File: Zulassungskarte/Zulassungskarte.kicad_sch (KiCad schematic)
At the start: 31 parts, among them J1 Conn_02x04_Counter_Clockwise, J2 Conn_02x04_Counter_Clockwise, U1 ATmega48V-10AU

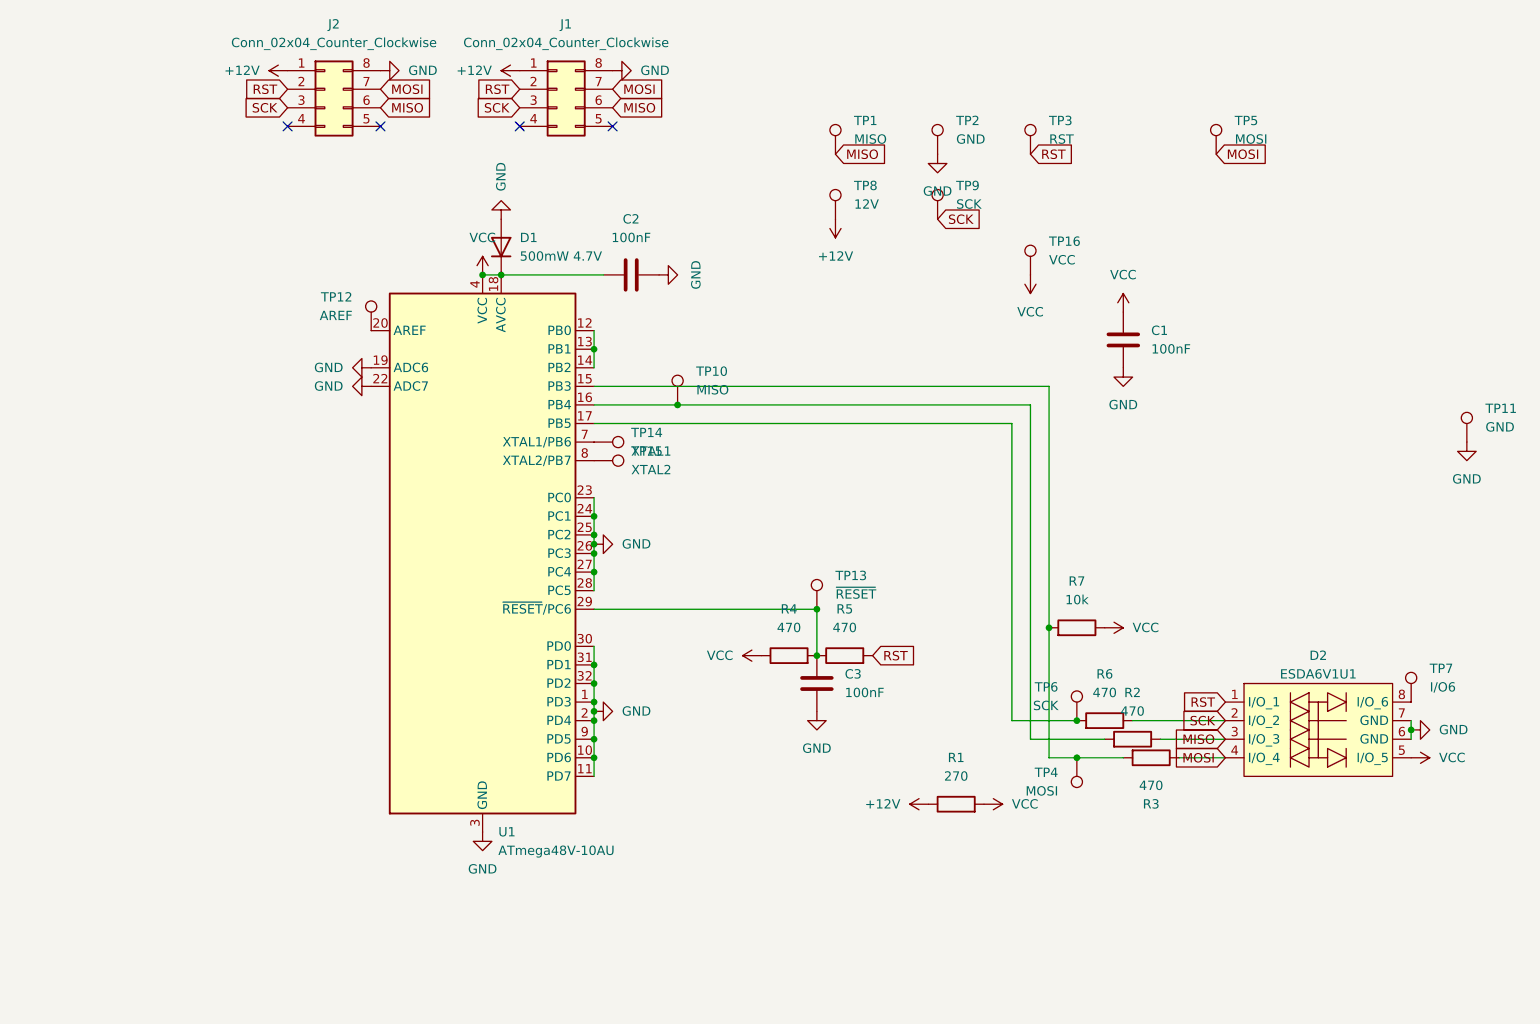
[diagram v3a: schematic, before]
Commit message: arduino isp und anschluss der normal am halter ist
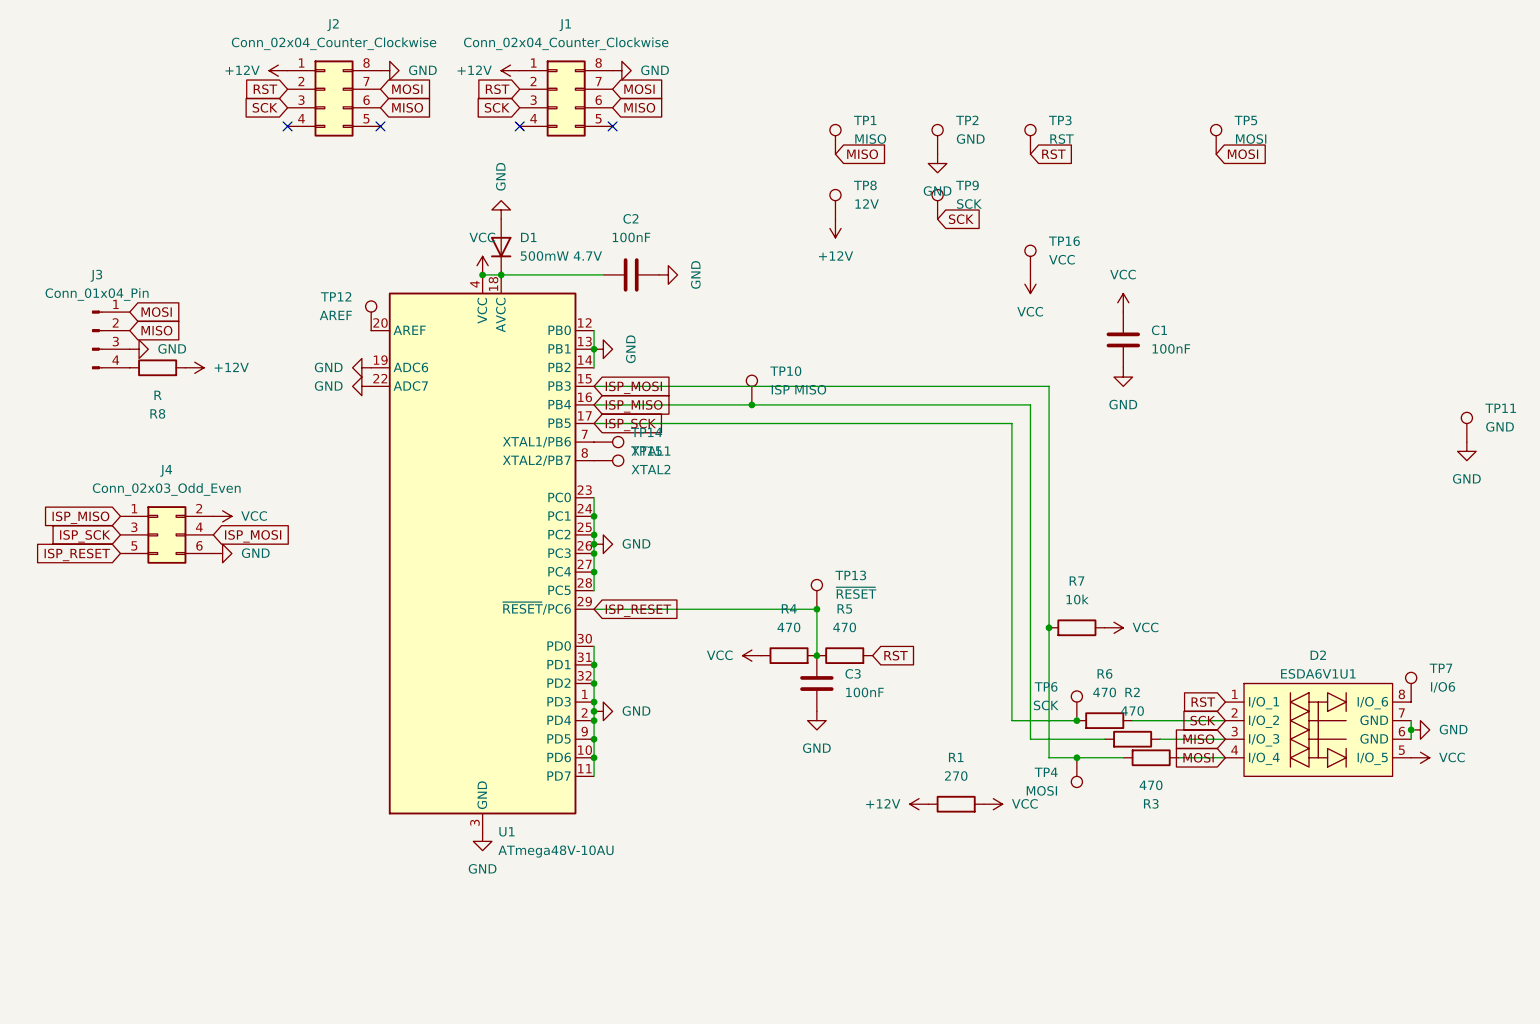
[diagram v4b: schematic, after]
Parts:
- added J3: Conn_01x04_Pin, Connector_JST:JST_XH_S4B-XH-A-1_1x04_P2.50mm_Horizontal, symbol Connector:Conn_01x04_Pin
- added J4: Conn_02x03_Odd_Even, Connector_IDC:IDC-Header_2x03_P2.54mm_Vertical, symbol Connector_Generic:Conn_02x03_Odd_Even
- added R8: R, Resistor_SMD:R_0805_2012Metric, symbol Device:R
- TP10: value MISO -> ISP MISO
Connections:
- net +12V: now also R8.2
- net GND: now also U1.12 (PB0), U1.13 (PB1), U1.14 (PB2), J3.3 (Pin_3), J4.6 (Pin_6)
- net MISO: now also J3.2 (Pin_2)
- net MOSI: now also J3.1 (Pin_1)
- net VCC: now also J4.2 (Pin_2)
- net ISP_MOSI: now reaches R3.2, R7.2, TP4.1, U1.15 (PB3)
- net ISP_MOSI: now also J4.4 (Pin_4)
- net ISP_MISO: now reaches R2.2, TP10.1, U1.16 (PB4)
- net ISP_MISO: now also J4.1 (Pin_1)
- net ISP_SCK: now reaches R6.2, TP6.1, U1.17 (PB5)
- net ISP_SCK: now also J4.3 (Pin_3)
- net ISP_RESET: now reaches C3.1, R4.2, R5.1, TP13.1, U1.29 (~{RESET}/PC6)
- net ISP_RESET: now also J4.5 (Pin_5)
- new net: J3.4 (Pin_4), R8.1
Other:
- moved on the sheet: TP10

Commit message: 5v und loecher
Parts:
- added FID1, FID2, FID3: Fiducial, Fiducial:Fiducial_0.75mm_Mask2.25mm, symbol Mechanical:Fiducial
- added H1, H2, H3: MountingHole, MountingHole:MountingHole_3.2mm_M3, symbol Mechanical:MountingHole
- J3: footprint Connector_JST:JST_XH_S4B-XH-A-1_1x04_P2.50mm_Horizontal -> Connector_PinHeader_2.54mm:PinHeader_1x04_P2.54mm_Vertical
- R8: footprint Resistor_SMD:R_0805_2012Metric -> Resistor_SMD:R_0603_1608Metric_Pad0.98x0.95mm_HandSolder
- TP14, TP15: footprint TestPoint:TestPoint_Pad_D1.5mm -> TestPoint:TestPoint_Pad_D1.0mm
- U1: value ATmega48V-10AU -> ATmega48
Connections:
- net +12V renamed +5V

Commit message: zlk
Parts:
- J3, J4: now not fitted
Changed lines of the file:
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@@
 		(in_bom yes)
 		(on_board yes)
-		(dnp no)
+		(dnp yes)
 		(fields_autoplaced yes)
 		(property "Reference" "J3"
@@
 		(in_bom yes)
 		(on_board yes)
-		(dnp no)
+		(dnp yes)
 		(fields_autoplaced yes)
 		(property "Reference" "J4"

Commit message: 12v zlk
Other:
- moved on the sheet: C2, D1
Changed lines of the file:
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@@
 	)
 	(junction
-		(at 72.39 49.53)
-		(diameter 0)
-		(color 0 0 0 0)
-	)
-	(junction
 		(at 87.63 59.69)
 		(diameter 0)
@@
 	)
 	(junction
-		(at 74.93 49.53)
+		(at 87.63 105.41)
 		(diameter 0)
 		(color 0 0 0 0)
 	)
 	(junction
-		(at 87.63 105.41)
+		(at 87.63 109.22)
 		(diameter 0)
 		(color 0 0 0 0)
 	)
 	(junction
-		(at 87.63 109.22)
+		(at 73.66 49.53)
 		(diameter 0)
 		(color 0 0 0 0)
@@
 	(wire
 		(pts
-			(xy 72.39 49.53) (xy 74.93 49.53)
-		)
-		(stroke
-			(width 0)
-			(type default)
-		)
-	)
-	(wire
-		(pts
 			(xy 157.48 113.03) (xy 147.32 113.03)
 		)
@@
 	(wire
 		(pts
-			(xy 87.63 100.33) (xy 87.63 102.87)
+			(xy 73.66 49.53) (xy 74.93 49.53)
 		)
 		(stroke
@@
 	(wire
 		(pts
-			(xy 87.63 90.17) (xy 87.63 92.71)
+			(xy 87.63 100.33) (xy 87.63 102.87)
 		)
 		(stroke
@@
 	(wire
 		(pts
-			(xy 74.93 49.53) (xy 88.9 49.53)
+			(xy 87.63 90.17) (xy 87.63 92.71)
 		)
 		(stroke
@@
 	(wire
 		(pts
+			(xy 73.66 49.53) (xy 72.39 49.53)
+		)
+		(stroke
+			(width 0)
+			(type default)
+		)
+	)
+	(wire
+		(pts
 			(xy 87.63 107.95) (xy 87.63 105.41)
 		)
@@
 	(symbol
 		(lib_id "power:GND")
-		(at 74.93 41.91 0)
+		(at 102.87 135.89 270)
 		(mirror x)
 		(unit 1)
@@
 		(fields_autoplaced yes)
 		(property "Reference" "#PWR024"
-			(at 74.93 35.56 0)
+			(at 96.52 135.89 0)
 			(effects
 				(font
@@
 		)
 		(property "Value" "GND"
-			(at 74.9301 38.1 90)
+			(at 99.06 135.8899 90)
 			(effects
 				(font
@@
 		)
 		(property "Footprint" ""
-			(at 74.93 41.91 0)
+			(at 102.87 135.89 0)
 			(effects
 				(font
@@
 		)
 		(property "Datasheet" ""
-			(at 74.93 41.91 0)
+			(at 102.87 135.89 0)
 			(effects
 				(font
@@
 		)
 		(property "Description" "Power symbol creates a global label with name \"GND\" , ground"
-			(at 74.93 41.91 0)
+			(at 102.87 135.89 0)
 			(effects
 				(font
@@
 	(symbol
 		(lib_id "power:VCC")
-		(at 72.39 49.53 0)
+		(at 73.66 49.53 0)
 		(unit 1)
 		(exclude_from_sim no)
@@
 		(fields_autoplaced yes)
 		(property "Reference" "#PWR03"
-			(at 72.39 53.34 0)
+			(at 73.66 53.34 0)
 			(effects
 				(font
@@
 		)
 		(property "Value" "VCC"
-			(at 72.39 44.45 0)
+			(at 73.66 44.45 0)
 			(effects
 				(font
@@
 		)
 		(property "Footprint" ""
-			(at 72.39 49.53 0)
+			(at 73.66 49.53 0)
 			(effects
 				(font
@@
 		)
 		(property "Datasheet" ""
-			(at 72.39 49.53 0)
+			(at 73.66 49.53 0)
 			(effects
 				(font
@@
 		)
 		(property "Description" "Power symbol creates a global label with name \"VCC\""
-			(at 72.39 49.53 0)
+			(at 73.66 49.53 0)
 			(effects
 				(font
@@
 	)
 	(symbol
+		(lib_id "power:VCC")
+		(at 110.49 135.89 270)
+		(unit 1)
+		(exclude_from_sim no)
+		(in_bom yes)
+		(on_board yes)
+		(dnp no)
+		(fields_autoplaced yes)
+		(property "Reference" "#PWR08"
+			(at 106.68 135.89 0)
+			(effects
+				(font
+					(size 1.27 1.27)
+				)
+				(hide yes)
+			)
+		)
+		(property "Value" "VCC"
+			(at 114.3 135.8899 90)
+			(effects
+				(font
+					(size 1.27 1.27)
+				)
+				(justify left)
+			)
+		)
+		(property "Footprint" ""
+			(at 110.49 135.89 0)
+			(effects
+				(font
+					(size 1.27 1.27)
+				)
+				(hide yes)
+			)
+		)
+		(property "Datasheet" ""
+			(at 110.49 135.89 0)
+			(effects
+				(font
+					(size 1.27 1.27)
+				)
+				(hide yes)
+			)
+		)
+		(property "Description" "Power symbol creates a global label with name \"VCC\""
+			(at 110.49 135.89 0)
+			(effects
+				(font
+					(size 1.27 1.27)
+				)
+				(hide yes)
+			)
+		)
+		(pin "1"
+		)
+		(instances
+			(project "Zulassungskarte"
+				(path "/f437cf05-d297-460e-8639-991b777c08ac"
+					(reference "#PWR08")
+					(unit 1)
+				)
+			)
+		)
+	)
+	(symbol
 		(lib_id "power:GND")
 		(at 199.39 111.76 90)
@@
 	(symbol
 		(lib_id "Device:D")
-		(at 74.93 45.72 270)
-		(mirror x)
+		(at 106.68 135.89 0)
+		(mirror y)
 		(unit 1)
 		(exclude_from_sim no)
@@
 		(fields_autoplaced yes)
 		(property "Reference" "D1"
-			(at 77.47 44.4499 90)
+			(at 105.4099 133.35 90)
 			(effects
 				(font
@@
 		)
 		(property "Value" "500mW 4.7V"
-			(at 77.47 46.9899 90)
+			(at 107.9499 133.35 90)
 			(effects
 				(font
@@
 		)
 		(property "Footprint" "Diode_SMD:D_SOD-123"
-			(at 74.93 45.72 0)
+			(at 106.68 135.89 0)
 			(effects
 				(font
@@
 		)
 		(property "Datasheet" "~"
-			(at 74.93 45.72 0)
+			(at 106.68 135.89 0)
 			(effects
 				(font
@@
 		)
 		(property "Description" "Diode"
-			(at 74.93 45.72 0)
+			(at 106.68 135.89 0)
 			(effects
 				(font
@@
 		)
 		(property "Sim.Device" "D"
-			(at 74.93 45.72 0)
+			(at 106.68 135.89 0)
 			(effects
 				(font
@@
 		)
 		(property "Sim.Pins" "1=K 2=A"
-			(at 74.93 45.72 0)
+			(at 106.68 135.89 0)
 			(effects
 				(font
@@
 	(symbol
 		(lib_id "Device:C")
-		(at 92.71 49.53 90)
+		(at 173.99 58.42 0)
 		(unit 1)
 		(exclude_from_sim no)
@@
 		(fields_autoplaced yes)
 		(property "Reference" "C2"
-			(at 92.71 41.91 90)
+			(at 181.61 58.42 90)
 			(effects
 				(font
@@
 		)
 		(property "Value" "100nF"
-			(at 92.71 44.45 90)
+			(at 179.07 58.42 90)
 			(effects
 				(font
@@
 		)
 		(property "Footprint" "Capacitor_SMD:C_0805_2012Metric_Pad1.18x1.45mm_HandSolder"
-			(at 96.52 48.5648 0)
+			(at 174.9552 62.23 0)
 			(effects
 				(font
@@
 		)
 		(property "Datasheet" "~"
-			(at 92.71 49.53 0)
+			(at 173.99 58.42 0)
 			(effects
 				(font
@@
 		)
 		(property "Description" "Unpolarized capacitor"
-			(at 92.71 49.53 0)
+			(at 173.99 58.42 0)
 			(effects
 				(font
@@
 	)
 	(symbol
+		(lib_id "power:VCC")
+		(at 173.99 54.61 0)
+		(unit 1)
+		(exclude_from_sim no)
+		(in_bom yes)
+		(on_board yes)
+		(dnp no)
+		(fields_autoplaced yes)
+		(property "Reference" "#PWR019"
+			(at 173.99 58.42 0)
+			(effects
+				(font
+					(size 1.27 1.27)
+				)
+				(hide yes)
+			)
+		)
+		(property "Value" "VCC"
+			(at 173.9901 50.8 90)
+			(effects
+				(font
+					(size 1.27 1.27)
+				)
+				(justify left)
+			)
+		)
+		(property "Footprint" ""
+			(at 173.99 54.61 0)
+			(effects
+				(font
+					(size 1.27 1.27)
+				)
+				(hide yes)
+			)
+		)
+		(property "Datasheet" ""
+			(at 173.99 54.61 0)
+			(effects
+				(font
+					(size 1.27 1.27)
+				)
+				(hide yes)
+			)
+		)
+		(property "Description" "Power symbol creates a global label with name \"VCC\""
+			(at 173.99 54.61 0)
+			(effects
+				(font
+					(size 1.27 1.27)
+				)
+				(hide yes)
+			)
+		)
+		(pin "1"
+		)
+		(instances
+			(project "Zulassungskarte"
+				(path "/f437cf05-d297-460e-8639-991b777c08ac"
+					(reference "#PWR019")
+					(unit 1)
+				)
+			)
+		)
+	)
+	(symbol
 		(lib_id "power:GND")
-		(at 96.52 49.53 90)
+		(at 173.99 62.23 0)
 		(unit 1)
 		(exclude_from_sim no)
@@
 		(fields_autoplaced yes)
 		(property "Reference" "#PWR010"
-			(at 102.87 49.53 0)
+			(at 173.99 68.58 0)
 			(effects
 				(font
@@
 		)
 		(property "Value" "GND"
-			(at 101.6 49.53 0)
+			(at 173.99 67.31 0)
 			(effects
 				(font
@@
 		)
 		(property "Footprint" ""
-			(at 96.52 49.53 0)
+			(at 173.99 62.23 0)
 			(effects
 				(font
@@
 		)
 		(property "Datasheet" ""
-			(at 96.52 49.53 0)
+			(at 173.99 62.23 0)
 			(effects
 				(font
@@
 		)
 		(property "Description" "Power symbol creates a global label with name \"GND\" , ground"
-			(at 96.52 49.53 0)
+			(at 173.99 62.23 0)
 			(effects
 				(font

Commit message: zlk widerstand
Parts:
- J3, J4: now left out of the parts list
- R4: value 470 -> 10k
- R8: value R -> 270; now not fitted; now left out of the parts list
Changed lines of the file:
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@@
 		(unit 1)
 		(exclude_from_sim no)
-		(in_bom yes)
-		(on_board yes)
-		(dnp no)
+		(in_bom no)
+		(on_board yes)
+		(dnp yes)
 		(property "Reference" "R8"
 			(at 27.94 68.58 90)
@@
 			)
 		)
-		(property "Value" "R"
+		(property "Value" "270"
 			(at 27.94 66.04 90)
 			(effects
@@
 		(unit 1)
 		(exclude_from_sim no)
-		(in_bom yes)
+		(in_bom no)
 		(on_board yes)
 		(dnp yes)
@@
 		(unit 1)
 		(exclude_from_sim no)
-		(in_bom yes)
+		(in_bom no)
 		(on_board yes)
 		(dnp yes)
@@
 			)
 		)
-		(property "Value" "470"
+		(property "Value" "10k"
 			(at 114.3 97.79 90)
 			(effects
